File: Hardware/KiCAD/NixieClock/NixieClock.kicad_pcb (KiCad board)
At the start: 2 copper layers, 232.9 x 65.8 mm, 37 parts, among them IC1 , IC2 

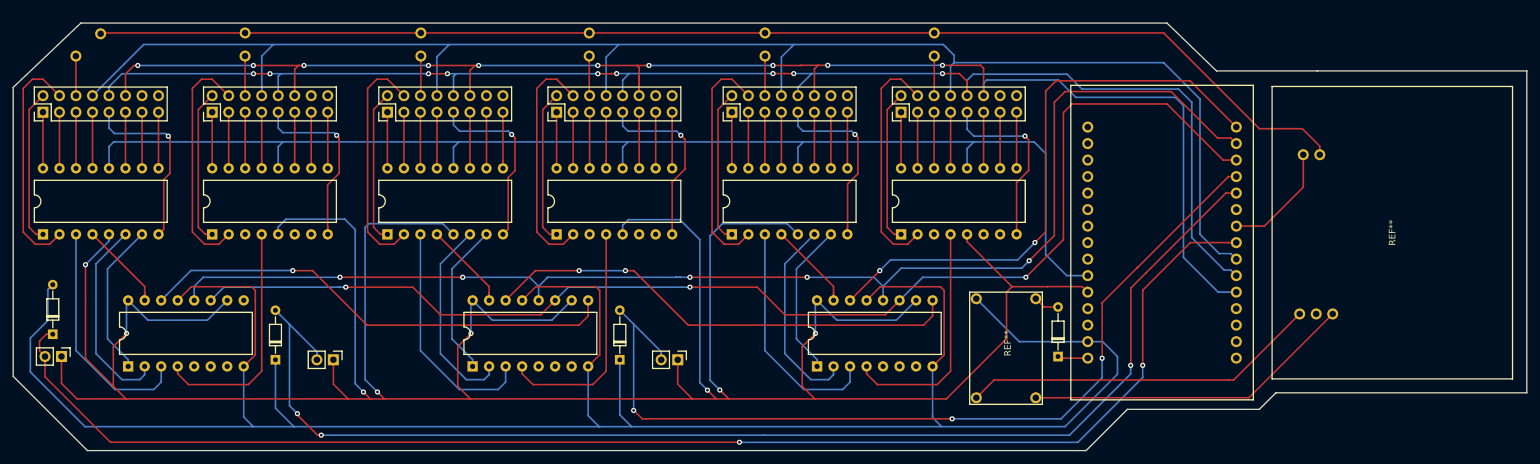
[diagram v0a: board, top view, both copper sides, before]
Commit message: Routed RGB LED resistors
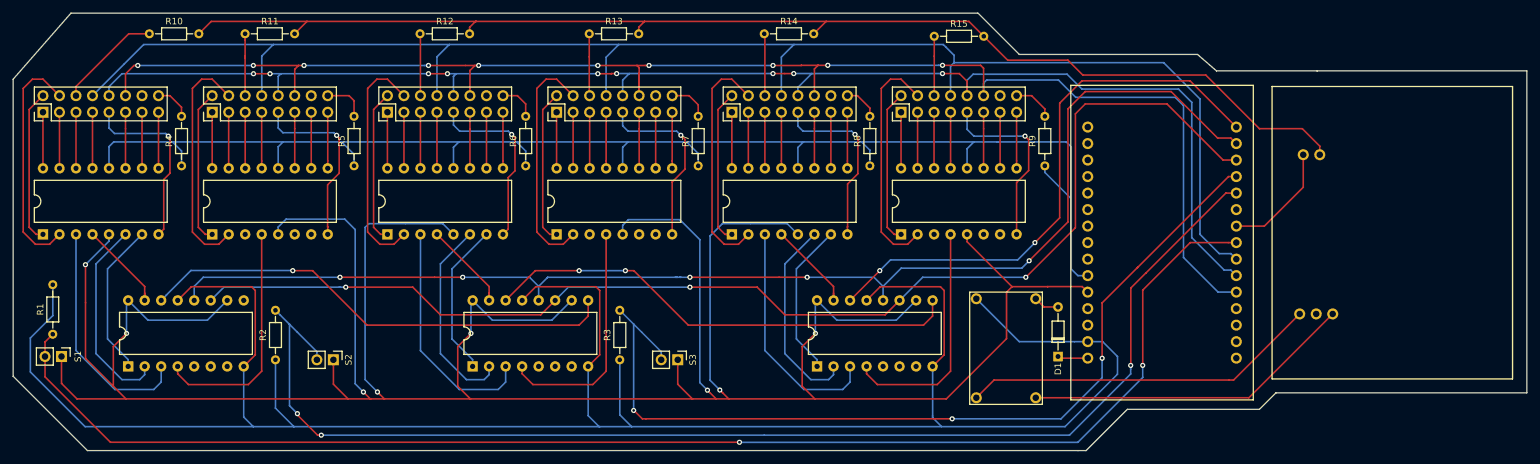
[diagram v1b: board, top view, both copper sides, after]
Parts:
- removed the   at (84.6, 77.7)
- removed the   at (190.6, 74.2)
- removed the   at (216.7, 77.7)
- removed the   at (216.7, 74.2)
- removed the   at (81.0, 120.5)
- removed the   at (82.4, 124.0)
- removed the   at (115.3, 124.5)
- removed the   at (124.2, 124.5)
- removed the   at (168.3, 124.5)
- removed the   at (88.4, 74.3)
- removed the   at (110.6, 77.7)
- removed the   at (110.6, 74.2)
- removed the   at (137.7, 77.7)
- removed the   at (137.7, 74.2)
- removed the   at (163.6, 77.7)
- removed the   at (163.6, 74.2)
- removed the   at (190.6, 77.7)
- added R1: 10K, Resistor_THT:R_Axial_DIN0204_L3.6mm_D1.6mm_P7.62mm_Horizontal, F.Cu at (81.0, 120.5)
- added R10: 30K, Resistor_THT:R_Axial_DIN0204_L3.6mm_D1.6mm_P7.62mm_Horizontal, F.Cu at (95.9, 74.3)
- added R11: 30K, Resistor_THT:R_Axial_DIN0204_L3.6mm_D1.6mm_P7.62mm_Horizontal, F.Cu at (110.6, 74.3)
- added R12: 30K, Resistor_THT:R_Axial_DIN0204_L3.6mm_D1.6mm_P7.62mm_Horizontal, F.Cu at (137.5, 74.3)
- added R13: 30K, Resistor_THT:R_Axial_DIN0204_L3.6mm_D1.6mm_P7.62mm_Horizontal, F.Cu at (163.6, 74.3)
- added R14: 30K, Resistor_THT:R_Axial_DIN0204_L3.6mm_D1.6mm_P7.62mm_Horizontal, F.Cu at (190.5, 74.3)
- added R15: 30K, Resistor_THT:R_Axial_DIN0204_L3.6mm_D1.6mm_P7.62mm_Horizontal, F.Cu at (216.7, 74.7)
- added R2: 10K, Resistor_THT:R_Axial_DIN0204_L3.6mm_D1.6mm_P7.62mm_Horizontal, F.Cu at (115.3, 124.5)
- added R3: 10K, Resistor_THT:R_Axial_DIN0204_L3.6mm_D1.6mm_P7.62mm_Horizontal, F.Cu at (168.3, 124.5)
- added R4: 300, Resistor_THT:R_Axial_DIN0204_L3.6mm_D1.6mm_P7.62mm_Horizontal, F.Cu at (100.8, 94.6)
- added R5: 300, Resistor_THT:R_Axial_DIN0204_L3.6mm_D1.6mm_P7.62mm_Horizontal, F.Cu at (127.4, 94.6)
- added R6: 300, Resistor_THT:R_Axial_DIN0204_L3.6mm_D1.6mm_P7.62mm_Horizontal, F.Cu at (153.8, 94.6)
- added R7: 300, Resistor_THT:R_Axial_DIN0204_L3.6mm_D1.6mm_P7.62mm_Horizontal, F.Cu at (180.3, 94.6)
- added R8: 300, Resistor_THT:R_Axial_DIN0204_L3.6mm_D1.6mm_P7.62mm_Horizontal, F.Cu at (206.8, 94.6)
- added R9: 300, Resistor_THT:R_Axial_DIN0204_L3.6mm_D1.6mm_P7.62mm_Horizontal, F.Cu at (233.7, 94.6)
- added S1: , Connector_PinHeader_2.54mm:PinHeader_1x02_P2.54mm_Vertical, F.Cu at (82.4, 124.0)
- added S2: , Connector_PinHeader_2.54mm:PinHeader_1x02_P2.54mm_Vertical, F.Cu at (124.2, 124.5)
-  : renamed from REF** (x3)
- D1, S3: renamed from  
- renumbered IC1 to IC2, IC1 to IC3, IC2 to IC4, IC2 to IC5, IC2 to IC6, IC2 to IC7, IC2 to IC8, IC2 to IC9
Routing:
- net (no net): track 4596.5 -> 4680.1 mm
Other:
- board size 232.9 x 65.8 mm -> 232.9 x 67.3 mm

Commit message: progress
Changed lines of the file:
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@@
     (thickness 1.6)
     (drawings 16)
-    (tracks 819)
+    (tracks 816)
     (zones 0)
     (modules 37)
@@
       (drillshape 0)
       (scaleselection 1)
-      (outputdirectory ""))
+      (outputdirectory "../Gerbers/"))
   )
   (net 0 "")
@@
   (segment (start 143.637 89.281) (end 142.68 88.324) (width 0.25) (layer B.Cu) (net 0))
   (segment (start 151.638 89.789) (end 151.13 89.281) (width 0.25) (layer B.Cu) (net 0))
-  (segment (start 123.335 104.02463) (end 123.317 104.00663) (width 0.25) (layer F.Cu) (net 0))
-  (segment (start 123.335 105.156) (end 123.335 104.02463) (width 0.25) (layer F.Cu) (net 0))
-  (segment (start 123.317 104.00663) (end 123.317 97.536) (width 0.25) (layer F.Cu) (net 0))
-  (segment (start 123.317 97.536) (end 125.095 95.758) (width 0.25) (layer F.Cu) (net 0))
-  (segment (start 125.095 95.758) (end 125.095 90.551) (width 0.25) (layer F.Cu) (net 0))
-  (segment (start 125.095 90.551) (end 125.095 90.297) (width 0.25) (layer F.Cu) (net 0))
   (via (at 124.714 89.916) (size 0.8) (drill 0.4) (layers F.Cu B.Cu) (net 0))
-  (segment (start 125.095 90.297) (end 124.714 89.916) (width 0.25) (layer F.Cu) (net 0))
   (segment (start 124.314001 89.516001) (end 116.440001 89.516001) (width 0.25) (layer B.Cu) (net 0))
   (segment (start 124.714 89.916) (end 124.314001 89.516001) (width 0.25) (layer B.Cu) (net 0))
@@
   (segment (start 221.996 72.39) (end 224.282 74.676) (width 0.25) (layer F.Cu) (net 0))
   (segment (start 200.025 72.39) (end 221.996 72.39) (width 0.25) (layer F.Cu) (net 0))
+  (segment (start 123.335 97.518) (end 123.335 105.156) (width 0.25) (layer F.Cu) (net 0))
+  (segment (start 125.095 95.758) (end 123.335 97.518) (width 0.25) (layer F.Cu) (net 0))
+  (segment (start 125.095 90.297) (end 125.095 95.758) (width 0.25) (layer F.Cu) (net 0))
+  (segment (start 124.714 89.916) (end 125.095 90.297) (width 0.25) (layer F.Cu) (net 0))
 )

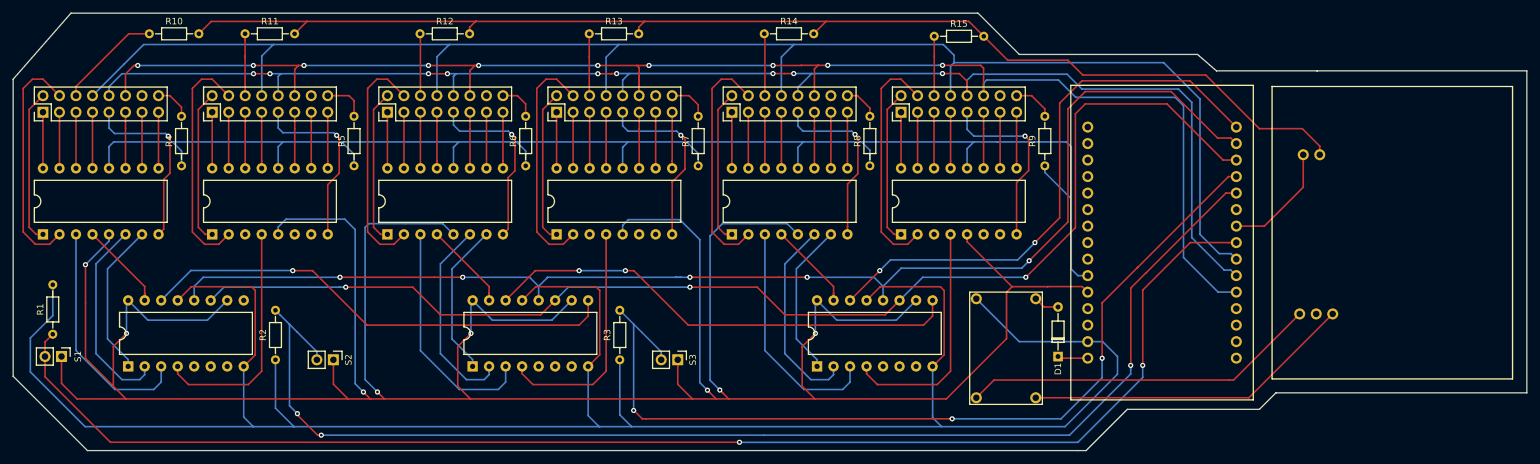
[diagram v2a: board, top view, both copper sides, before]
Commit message: started finishing routing to nixie driver chip.
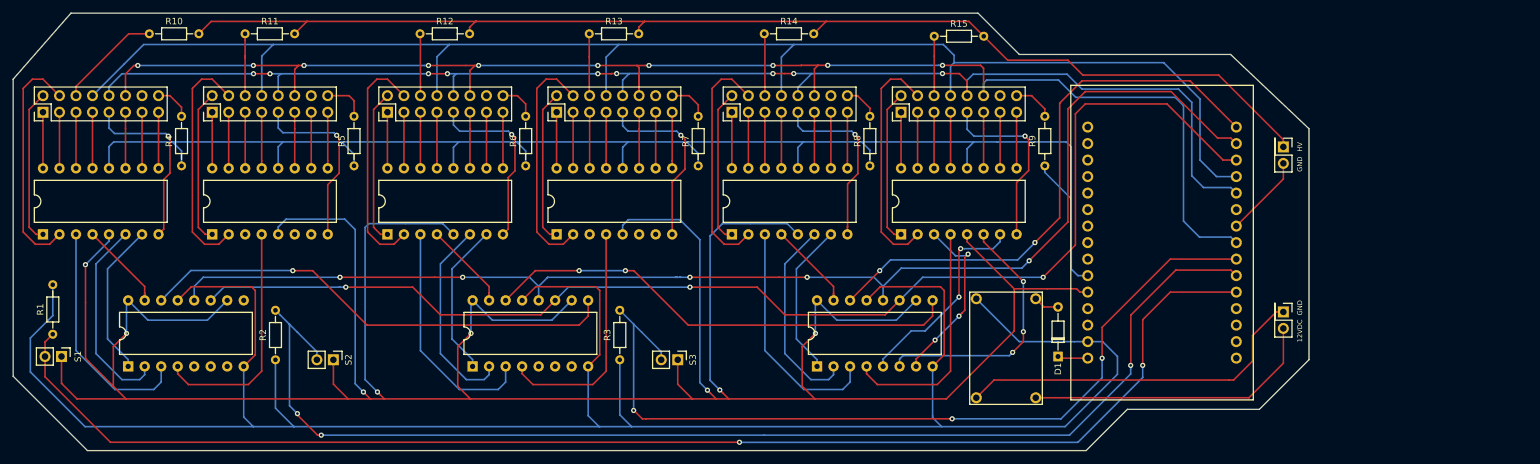
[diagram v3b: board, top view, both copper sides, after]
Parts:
- removed the   at (287.1, 104.9)
- added  : , Connector_PinHeader_2.54mm:PinHeader_2x01_P2.54mm_Vertical, F.Cu at (270.4, 117.1)
- added  : , Connector_PinHeader_2.54mm:PinHeader_2x01_P2.54mm_Vertical, F.Cu at (270.4, 91.7)
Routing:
- net (no net): track 4680.1 -> 4714.7 mm, vias 54 -> 62
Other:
- board size 232.9 x 67.3 mm -> 199.4 x 67.3 mm
- board text added: "12VDC"
- board text added: "GND"
- board text added: "HV"

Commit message: Finished routing all pins to BCD encoders
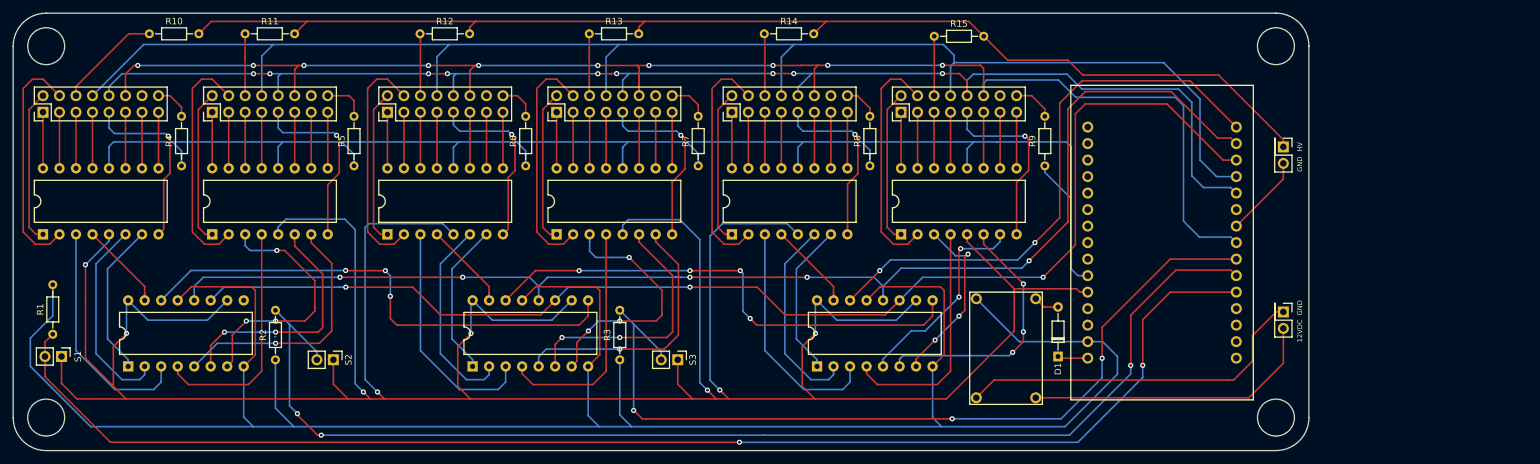
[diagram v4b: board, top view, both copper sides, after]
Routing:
- net (no net): track 4714.7 -> 4957.8 mm, vias 62 -> 78
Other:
- outline, holes or cut-outs redrawn

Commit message: done?
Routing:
- net (no net): track 4957.8 -> 4994.3 mm, vias 78 -> 77
